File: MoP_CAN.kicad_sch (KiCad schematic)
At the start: 15 parts, among them J16 CAN, U1 74LVC2G14, U2 74LVC2G14, U8 MCP2542FDxMF

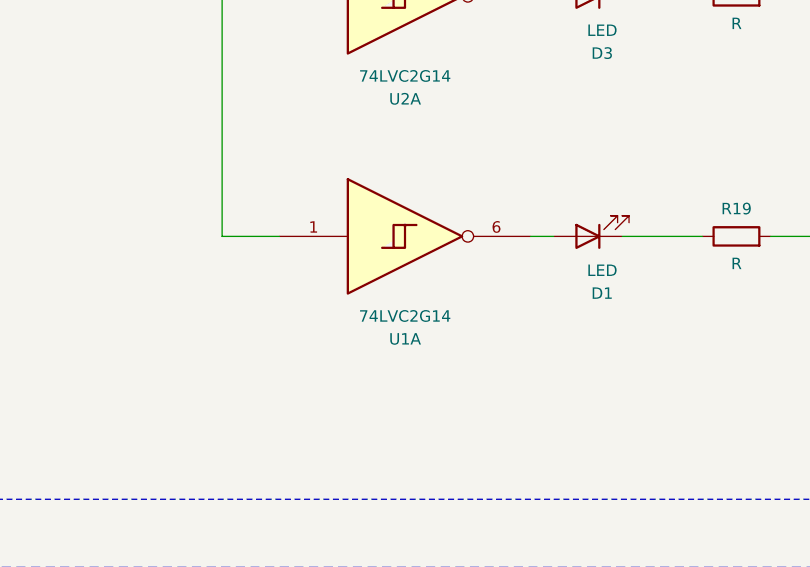
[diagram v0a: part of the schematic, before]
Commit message: changed ref designators to be consistent accross sheets
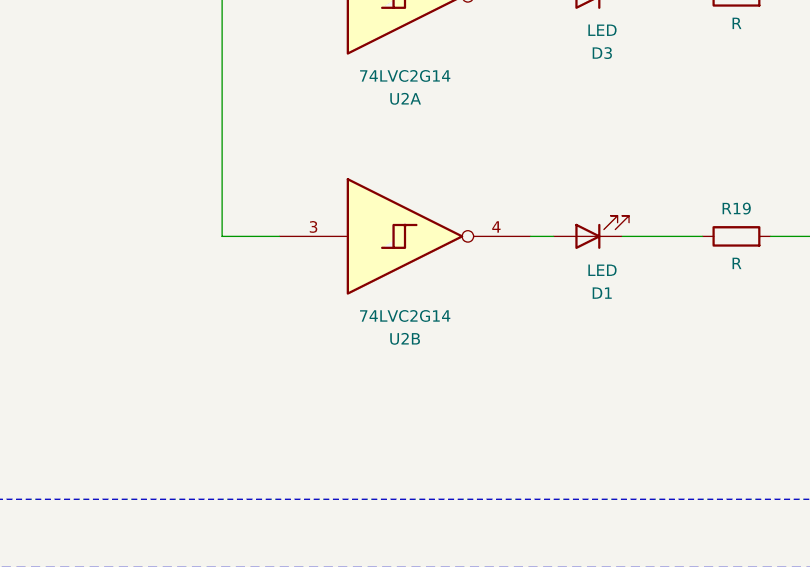
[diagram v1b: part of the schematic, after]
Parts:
- U8: footprint Package_DFN_QFN:DFN-8-1EP_3x3mm_P0.65mm_EP1.55x2.4mm -> Package_SO:SOIC-8-1EP_3.9x4.9mm_P1.27mm_EP2.41x3.3mm
- renumbered U1 to U2
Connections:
- net Tx: now also U2.3; no longer U2.1
- net at D1.2 (A): now also U2.4; no longer U2.6
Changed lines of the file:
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@@
 		(lib_id "74xGxx:74LVC2G14")
 		(at 104.14 123.19 0)
-		(unit 1)
-		(exclude_from_sim no)
-		(in_bom yes)
-		(on_board yes)
-		(dnp no)
-		(fields_autoplaced yes)
-		(property "Reference" "U1"
+		(unit 2)
+		(exclude_from_sim no)
+		(in_bom yes)
+		(on_board yes)
+		(dnp no)
+		(fields_autoplaced yes)
+		(property "Reference" "U2"
 			(at 102.87 134.62 0)
 			(effects
@@
 			(project "MoP"
 				(path "/4d76798e-9a11-4d8d-a723-72f274a89091/25fbd90b-9dc8-4814-b6c9-7fb5a2a8a262"
-					(reference "U1")
-					(unit 1)
+					(reference "U2")
+					(unit 2)
 				)
 			)
@@
 			)
 		)
-		(property "Footprint" "Package_DFN_QFN:DFN-8-1EP_3x3mm_P0.65mm_EP1.55x2.4mm"
+		(property "Footprint" "Package_SO:SOIC-8-1EP_3.9x4.9mm_P1.27mm_EP2.41x3.3mm"
 			(at 151.13 85.09 0)
 			(effects

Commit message: Finished schematics
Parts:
- removed U2: 74LVC2G14, symbol 74xGxx:74LVC2G14
- added U702: 74LVC2G14, Package_TO_SOT_SMD:SOT-23-6, symbol 74xGxx:74LVC2G14
- C701: renamed from C2; footprint (none) -> Capacitor_SMD:C_0805_2012Metric_Pad1.18x1.45mm_HandSolder
- C702: renamed from C1; footprint (none) -> Capacitor_SMD:C_0805_2012Metric_Pad1.18x1.45mm_HandSolder
- D701: renamed from D3; footprint (none) -> Diode_SMD:D_0805_2012Metric
- D702: renamed from D1; footprint (none) -> Diode_SMD:D_0805_2012Metric
- JP701: renamed from JP10; footprint (none) -> Connector_PinHeader_2.54mm:PinHeader_1x02_P2.54mm_Vertical
- JP702: renamed from JP11; footprint (none) -> Connector_PinHeader_2.54mm:PinHeader_1x02_P2.54mm_Vertical
- R701: renamed from R3; footprint (none) -> Resistor_SMD:R_0805_2012Metric; now not fitted
- R702: renamed from R4; footprint (none) -> Resistor_SMD:R_0805_2012Metric; now not fitted
- R703: renamed from R2; footprint (none) -> Resistor_SMD:R_0805_2012Metric
- R704: renamed from R12; footprint (none) -> Resistor_SMD:R_0805_2012Metric
- R705: renamed from R19; footprint (none) -> Resistor_SMD:R_0805_2012Metric
- renumbered J16 to J701, U8 to U701
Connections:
- net GND: now also U702.2 (GND)
- net Rx: now also U702.1
- net Tx: now also U702.3
- net at C702.1, JP701.2 (B), R701.2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: now also U702.5 (VCC)
- net at D702.2 (A): now also U702.4
- net at D701.2 (A): now also U702.6

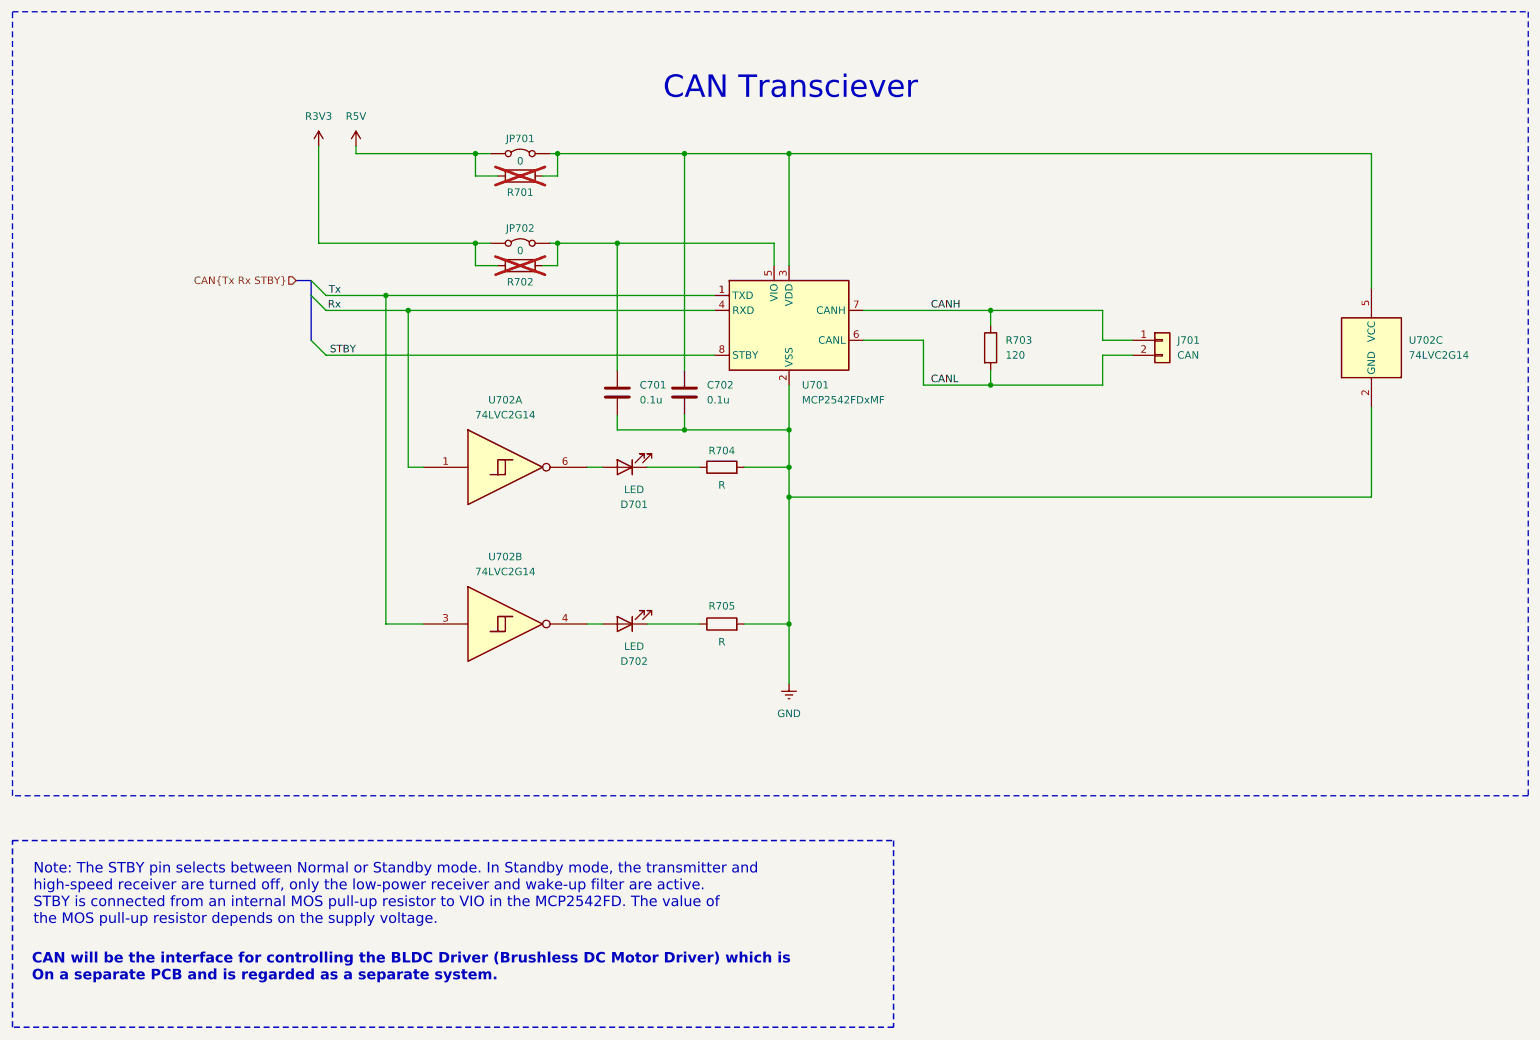
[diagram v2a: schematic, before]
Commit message: Added subproject for EPS PCB
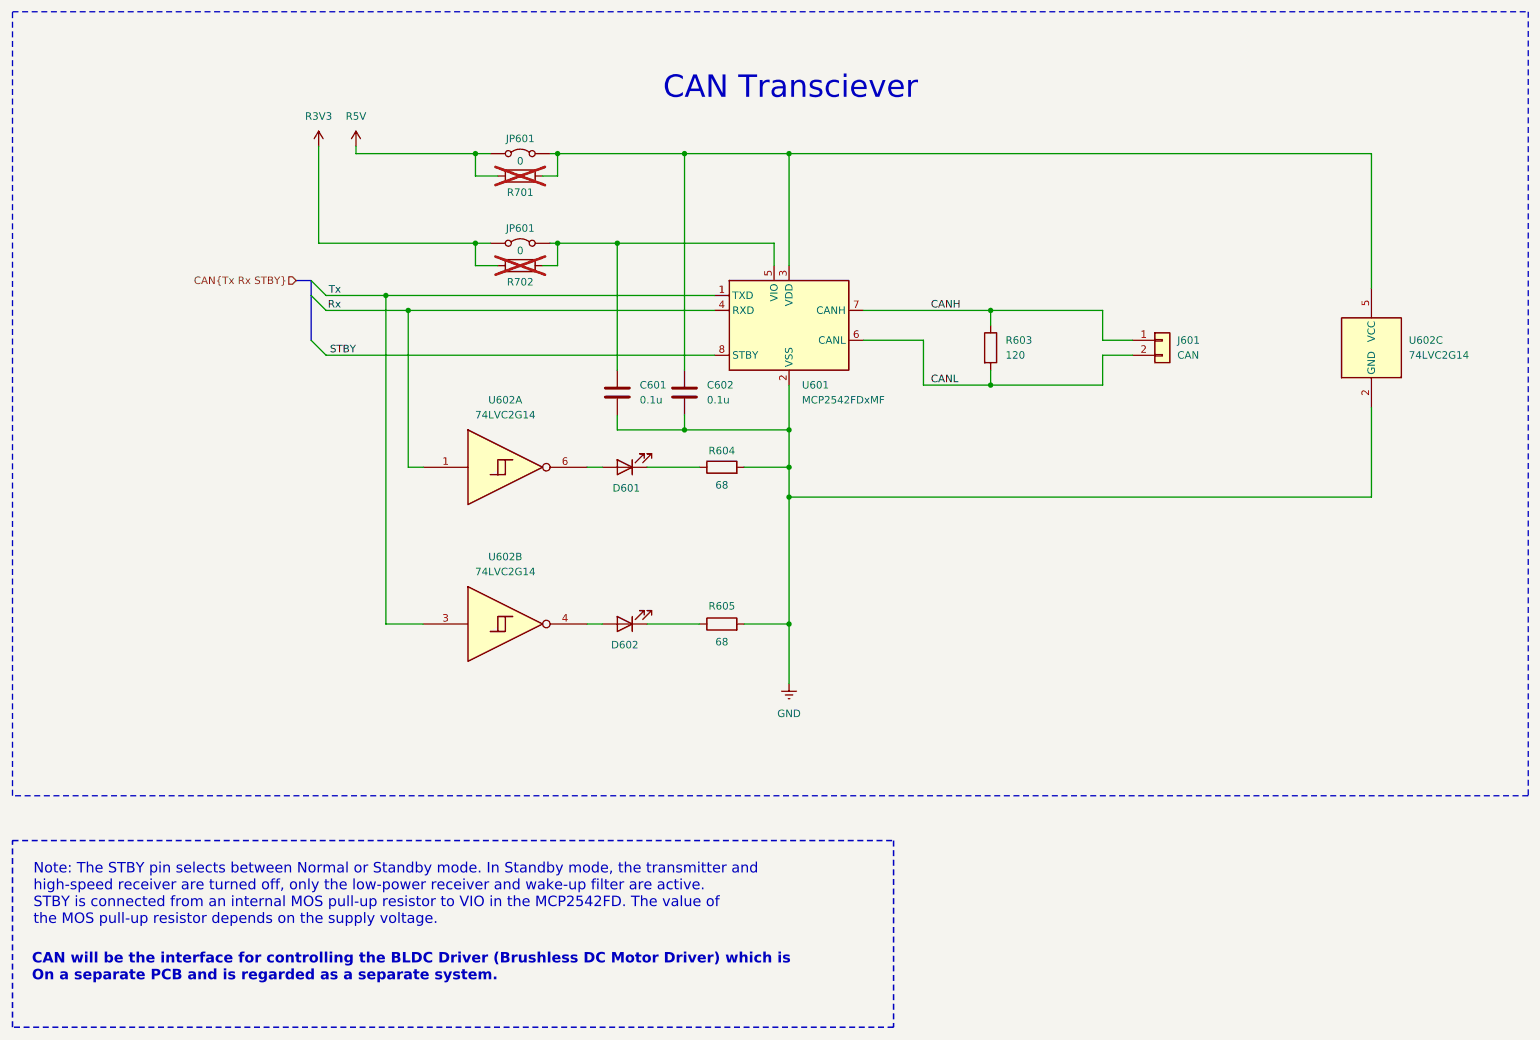
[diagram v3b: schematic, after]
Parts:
- D601: renamed from D701; value LED -> CMD17-21VGC/TR8
- D602: renamed from D702; value LED -> CMD17-21VGC/TR8
- J601: renamed from J701; footprint (none) -> Connector_PinHeader_2.54mm:PinHeader_1x02_P2.54mm_Vertical
- R604: renamed from R704; value R -> 68
- R605: renamed from R705; value R -> 68
- renumbered C701 to C601, C702 to C602, JP702 to JP601, JP701 to JP601, R703 to R603, U701 to U601, U702 to U602

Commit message: added OBC
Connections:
- net Rx renamed CAN.Rx
- net STBY renamed CAN.STBY
- net Tx renamed CAN.Tx
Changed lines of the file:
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@@
 		)
 	)
-	(label "STBY"
-		(at 77.47 77.47 180)
+	(label "CAN.STBY"
+		(at 81.28 77.47 180)
 		(fields_autoplaced yes)
 		(effects
@@
 		)
 	)
-	(label "Tx"
-		(at 74.93 67.31 180)
+	(label "CAN.Tx"
+		(at 78.74 67.31 180)
 		(fields_autoplaced yes)
 		(effects
@@
 		)
 	)
-	(label "Rx"
-		(at 74.93 69.85 180)
+	(label "CAN.Rx"
+		(at 78.74 69.85 180)
 		(fields_autoplaced yes)
 		(effects
@@
 				)
 			)
+			(project "MoP"
+				(path "/4fa4f4fb-851d-4975-b789-eb7f900188ea/2f2cb406-bfa1-4a41-902f-a9f1d7d0ee7f"
+					(reference "JP202")
+					(unit 1)
+				)
+			)
 		)
 	)
@@
 				)
 			)
+			(project ""
+				(path "/4fa4f4fb-851d-4975-b789-eb7f900188ea/2f2cb406-bfa1-4a41-902f-a9f1d7d0ee7f"
+					(reference "C202")
+					(unit 1)
+				)
+			)
 		)
 	)
@@
 				)
 			)
+			(project "MoP"
+				(path "/4fa4f4fb-851d-4975-b789-eb7f900188ea/2f2cb406-bfa1-4a41-902f-a9f1d7d0ee7f"
+					(reference "R702")
+					(unit 1)
+				)
+			)
 		)
 	)
@@
 				)
 			)
+			(project "MoP"
+				(path "/4fa4f4fb-851d-4975-b789-eb7f900188ea/2f2cb406-bfa1-4a41-902f-a9f1d7d0ee7f"
+					(reference "D202")
+					(unit 1)
+				)
+			)
 		)
 	)
@@
 				(path "/4d76798e-9a11-4d8d-a723-72f274a89091/25fbd90b-9dc8-4814-b6c9-7fb5a2a8a262"
 					(reference "R604")
+					(unit 1)
+				)
+			)
+			(project ""
+				(path "/4fa4f4fb-851d-4975-b789-eb7f900188ea/2f2cb406-bfa1-4a41-902f-a9f1d7d0ee7f"
+					(reference "R202")
 					(unit 1)
 				)
@@
 				)
 			)
+			(project "MoP"
+				(path "/4fa4f4fb-851d-4975-b789-eb7f900188ea/2f2cb406-bfa1-4a41-902f-a9f1d7d0ee7f"
+					(reference "JP201")
+					(unit 1)
+				)
+			)
 		)
 	)
@@
 				(path "/4d76798e-9a11-4d8d-a723-72f274a89091/25fbd90b-9dc8-4814-b6c9-7fb5a2a8a262"
 					(reference "D601")
+					(unit 1)
+				)
+			)
+			(project "MoP"
+				(path "/4fa4f4fb-851d-4975-b789-eb7f900188ea/2f2cb406-bfa1-4a41-902f-a9f1d7d0ee7f"
+					(reference "D201")
+					(unit 1)
+				)
+			)
+		)
+	)
+	(symbol
+		(lib_id "power:+5V")
+		(at 71.12 41.91 0)
+		(unit 1)
+		(exclude_from_sim no)
+		(in_bom yes)
+		(on_board yes)
+		(dnp no)
+		(fields_autoplaced yes)
+		(property "Reference" "#PWR0201"
+			(at 71.12 45.72 0)
+			(effects
+				(font
+					(size 1.27 1.27)
+				)
+				(hide yes)
+			)
+		)
+		(property "Value" "R3V3"
+			(at 71.12 36.83 0)
+			(effects
+				(font
+					(size 1.27 1.27)
+				)
+			)
+		)
+		(property "Footprint" ""
+			(at 71.12 41.91 0)
+			(effects
+				(font
+					(size 1.27 1.27)
+				)
+				(hide yes)
+			)
+		)
+		(property "Datasheet" ""
+			(at 71.12 41.91 0)
+			(effects
+				(font
+					(size 1.27 1.27)
+				)
+				(hide yes)
+			)
+		)
+		(property "Description" "Power symbol creates a global label with name \"+5V\""
+			(at 71.12 41.91 0)
+			(effects
+				(font
+					(size 1.27 1.27)
+				)
+				(hide yes)
+			)
+		)
+		(pin "1"
+		)
+		(instances
+			(project "OBC"
+				(path "/4fa4f4fb-851d-4975-b789-eb7f900188ea/2f2cb406-bfa1-4a41-902f-a9f1d7d0ee7f"
+					(reference "#PWR0201")
 					(unit 1)
 				)
@@
 				)
 			)
+			(project "MoP"
+				(path "/4fa4f4fb-851d-4975-b789-eb7f900188ea/2f2cb406-bfa1-4a41-902f-a9f1d7d0ee7f"
+					(reference "C201")
+					(unit 1)
+				)
+			)
 		)
 	)
@@
 				)
 			)
+			(project "MoP"
+				(path "/4fa4f4fb-851d-4975-b789-eb7f900188ea/2f2cb406-bfa1-4a41-902f-a9f1d7d0ee7f"
+					(reference "U201")
+					(unit 1)
+				)
+			)
 		)
 	)
@@
 		(dnp no)
 		(fields_autoplaced yes)
-		(property "Reference" "#PWR024"
+		(property "Reference" "#PWR0202"
 			(at 77.47 45.72 0)
 			(effects
@@
 		)
 		(instances
-			(project ""
-				(path "/4d76798e-9a11-4d8d-a723-72f274a89091/25fbd90b-9dc8-4814-b6c9-7fb5a2a8a262"
-					(reference "#PWR024")
+			(project "OBC"
+				(path "/4fa4f4fb-851d-4975-b789-eb7f900188ea/2f2cb406-bfa1-4a41-902f-a9f1d7d0ee7f"
+					(reference "#PWR0202")
 					(unit 1)
 				)
@@
 				(path "/4d76798e-9a11-4d8d-a723-72f274a89091/25fbd90b-9dc8-4814-b6c9-7fb5a2a8a262"
 					(reference "R605")
+					(unit 1)
+				)
+			)
+			(project ""
+				(path "/4fa4f4fb-851d-4975-b789-eb7f900188ea/2f2cb406-bfa1-4a41-902f-a9f1d7d0ee7f"
+					(reference "R203")
 					(unit 1)
 				)
@@
 				)
 			)
+			(project ""
+				(path "/4fa4f4fb-851d-4975-b789-eb7f900188ea/2f2cb406-bfa1-4a41-902f-a9f1d7d0ee7f"
+					(reference "J201")
+					(unit 1)
+				)
+			)
 		)
 	)
@@
 				)
 			)
-		)
-	)
-	(symbol
-		(lib_id "power:+3V3")
-		(at 71.12 41.91 0)
-		(unit 1)
-		(exclude_from_sim no)
-		(in_bom yes)
-		(on_board yes)
-		(dnp no)
-		(fields_autoplaced yes)
-		(property "Reference" "#PWR025"
-			(at 71.12 45.72 0)
-			(effects
-				(font
-					(size 1.27 1.27)
-				)
-				(hide yes)
-			)
-		)
-		(property "Value" "R3V3"
-			(at 71.12 36.83 0)
-			(effects
-				(font
-					(size 1.27 1.27)
-				)
-			)
-		)
-		(property "Footprint" ""
-			(at 71.12 41.91 0)
-			(effects
-				(font
-					(size 1.27 1.27)
-				)
-				(hide yes)
-			)
-		)
-		(property "Datasheet" ""
-			(at 71.12 41.91 0)
-			(effects
-				(font
-					(size 1.27 1.27)
-				)
-				(hide yes)
-			)
-		)
-		(property "Description" "Power symbol creates a global label with name \"+3V3\""
-			(at 71.12 41.91 0)
-			(effects
-				(font
-					(size 1.27 1.27)
-				)
-				(hide yes)
-			)
-		)
-		(pin "1"
-		)
-		(instances
-			(project ""
-				(path "/4d76798e-9a11-4d8d-a723-72f274a89091/25fbd90b-9dc8-4814-b6c9-7fb5a2a8a262"
-					(reference "#PWR025")
-					(unit 1)
+			(project "MoP"
+				(path "/4fa4f4fb-851d-4975-b789-eb7f900188ea/2f2cb406-bfa1-4a41-902f-a9f1d7d0ee7f"
+					(reference "U202")
+					(unit 2)
 				)
 			)
@@
 				)
 			)
+			(project ""
+				(path "/4fa4f4fb-851d-4975-b789-eb7f900188ea/2f2cb406-bfa1-4a41-902f-a9f1d7d0ee7f"
+					(reference "#PWR07")
+					(unit 1)
+				)
+			)
 		)
 	)
@@
 			(project "MoP"
 				(path "/4d76798e-9a11-4d8d-a723-72f274a89091/25fbd90b-9dc8-4814-b6c9-7fb5a2a8a262"
+					(reference "R701")
+					(unit 1)
+				)
+			)
+			(project "MoP"
+				(path "/4fa4f4fb-851d-4975-b789-eb7f900188ea/2f2cb406-bfa1-4a41-902f-a9f1d7d0ee7f"
 					(reference "R701")
 					(unit 1)
@@
 				)
 			)
+			(project "MoP"
+				(path "/4fa4f4fb-851d-4975-b789-eb7f900188ea/2f2cb406-bfa1-4a41-902f-a9f1d7d0ee7f"
+					(reference "U202")
+					(unit 1)
+				)
+			)
 		)
 	)
@@
 				)
 			)
+			(project "MoP"
+				(path "/4fa4f4fb-851d-4975-b789-eb7f900188ea/2f2cb406-bfa1-4a41-902f-a9f1d7d0ee7f"
+					(reference "U202")
+					(unit 3)
+				)
+			)
 		)
 	)
@@
 					(unit 1)
 				)
+			)
+			(project "MoP"
+				(path "/4fa4f4fb-851d-4975-b789-eb7f900188ea/2f2cb406-bfa1-4a41-902f-a9f1d7d0ee7f"
+					(reference "R201")
+					(unit 1)
+				)
